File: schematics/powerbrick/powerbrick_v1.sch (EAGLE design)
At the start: 41 parts, among them U1 ATXMEGA128C3-AU, U2 TC1262-3.3VDB, U3 PRTR5V0U2X, U4 ULN2003LVPWR, U5 MCP9800A0T-M/OT

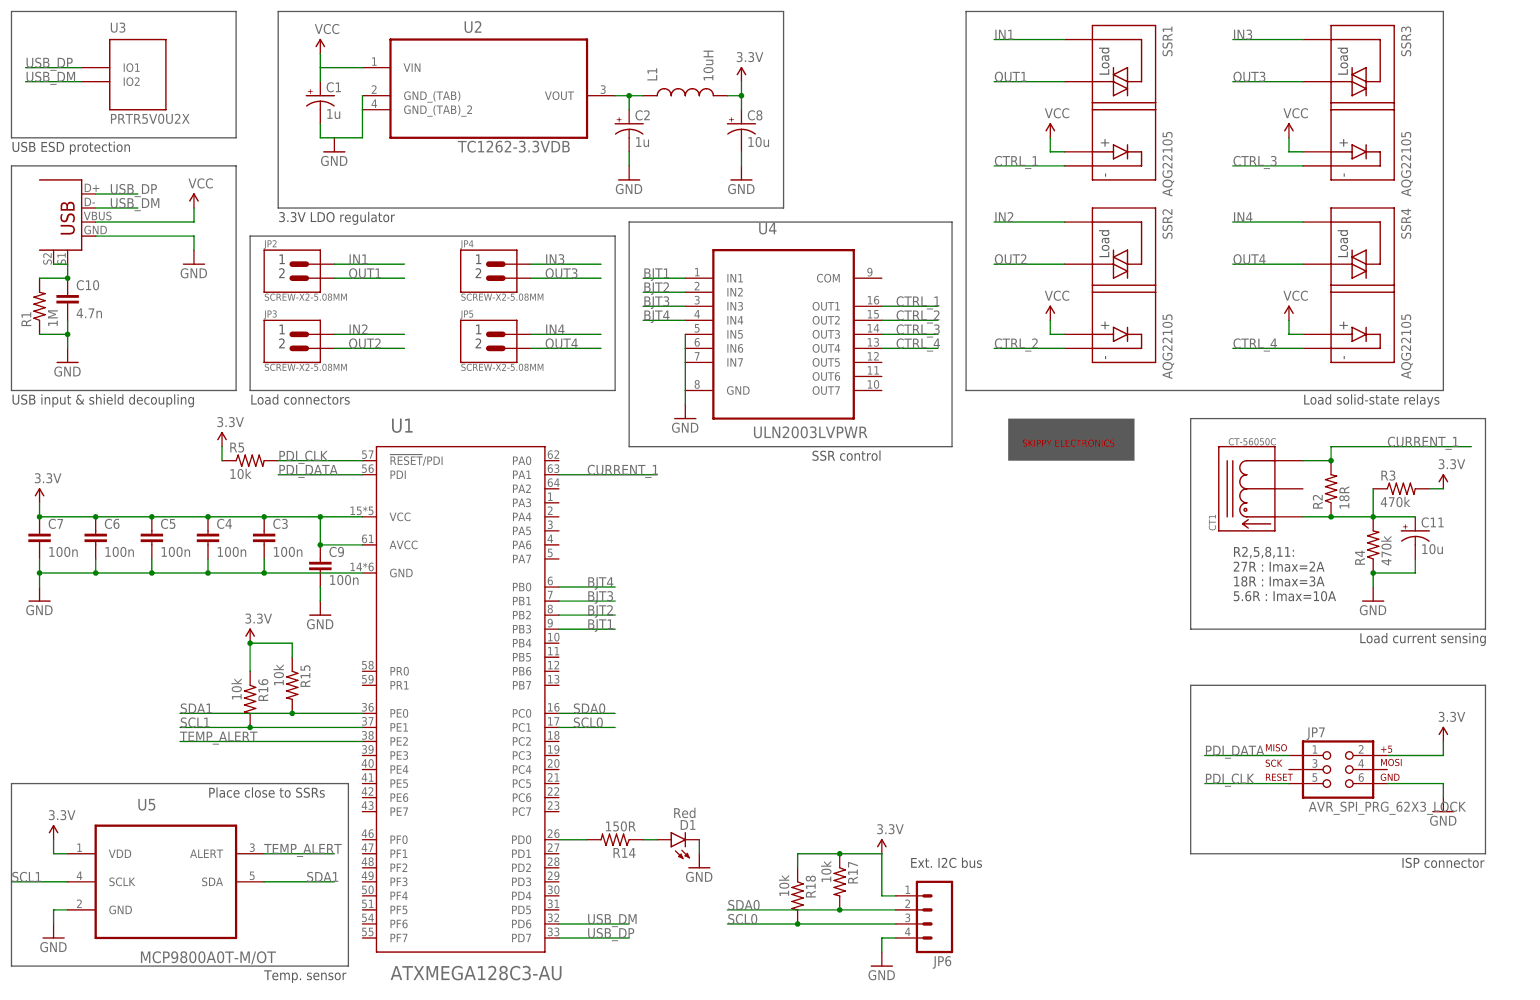
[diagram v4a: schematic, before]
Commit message: Replaced ISP connector - PCB draft
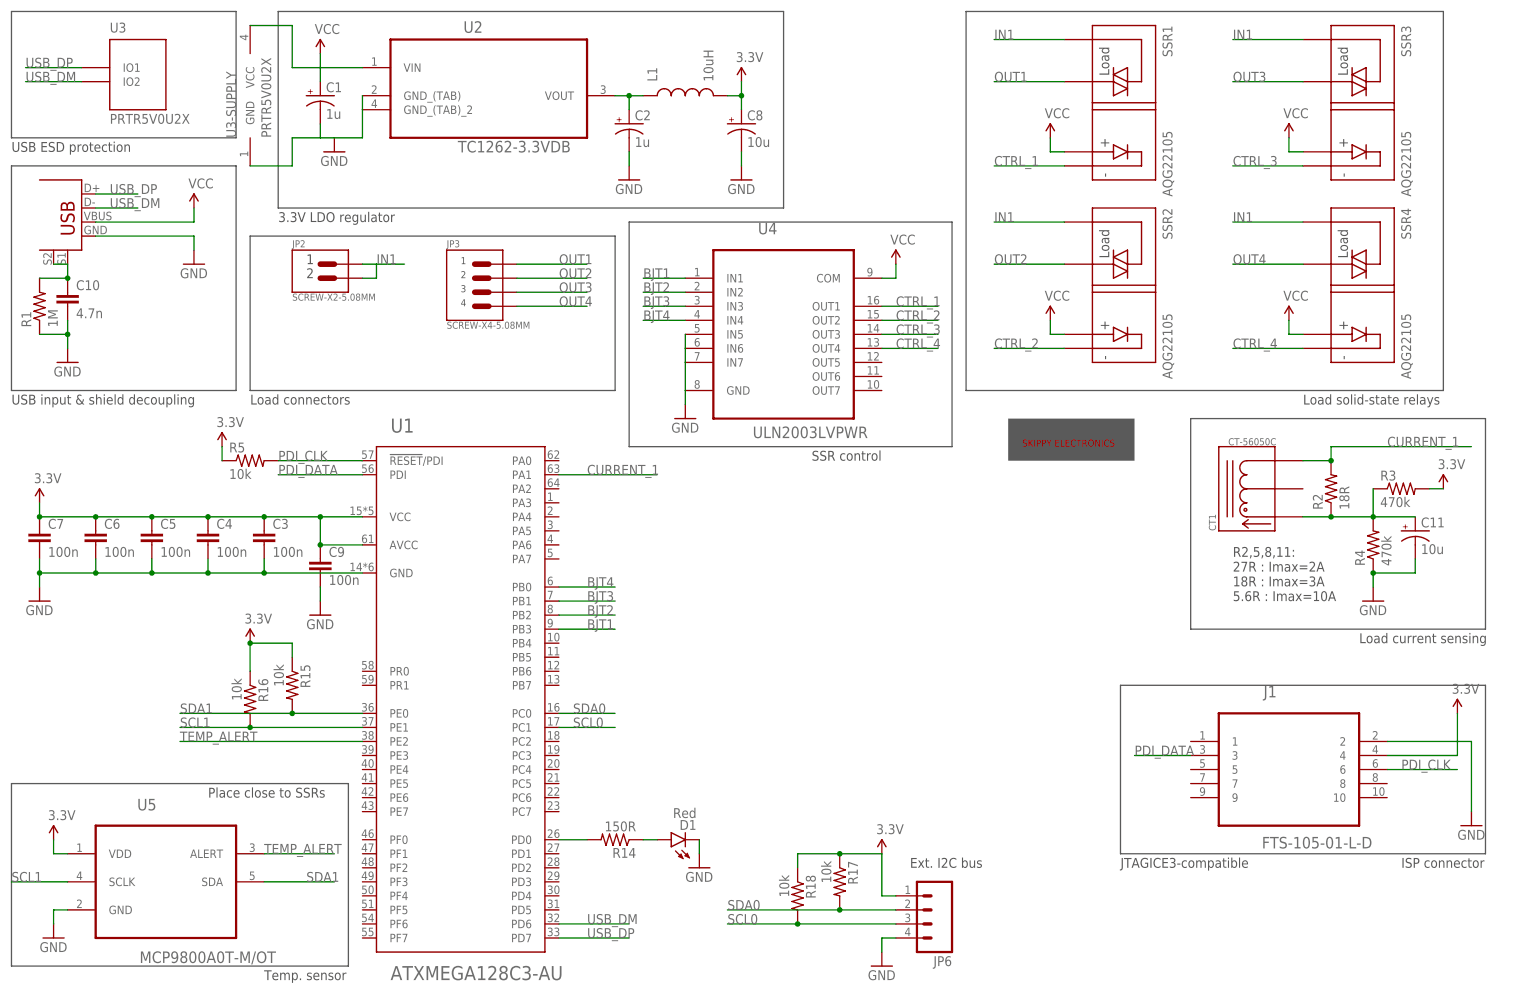
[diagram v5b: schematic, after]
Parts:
- removed JP4, JP5: SCREW-X2-5.08MM, Skippy-Connectors:SCREW-X2-5.08MM
- removed JP7: AVR_SPI_PRG_62X3_LOCK, SparkFun-Connectors:AVR_SPI_PRG_62X3_LOCK
- added J1: FTS-105-01-L-D, Skippy-Connectors:FTS-105-01-L-D
- JP3: value SCREW-X2-5.08MM -> SCREW-X4-5.08MM; device Skippy-Connectors:SCREW-X2-5.08MM -> Skippy-Connectors:SCREW-X4-5.08MM; OC_FARNELL 2315273 -> 2315275
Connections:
- removed net IN2: JP3.P$1, SSR2.P$1
- removed net IN3: JP4.P$1, SSR3.P$1
- removed net IN4: JP5.P$1, SSR4.P$1
- net 3.3V: now also J1.4; no longer JP7.2
- net GND: now also J1.2, U3-SUPPLY.GND; no longer JP7.6
- net IN1: now also JP2.P$2, SSR2.P$1, SSR3.P$1, SSR4.P$1
- net OUT1: now also JP3.P$1; no longer JP2.P$2
- net OUT3: now also JP3.P$3; no longer JP4.P$2
- net OUT4: now also JP3.P$4; no longer JP5.P$2
- net PDI_CLK: now also J1.6; no longer JP7.5
- net PDI_DATA: now also J1.3; no longer JP7.1
- net VCC: now also U3-SUPPLY.VCC, U4.COM
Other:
- note added: "JTAGICE3-compatible"
- moved on the sheet: JP2

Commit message: Added test points and HV separation milling
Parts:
- added C12, C13: 18p, SparkFun-Capacitors:CAP0805
- added R6, R7, R8, R9: Unfit, SparkFun-Passives:RESISTOR0805-RES
- added TP1, TP2, TP3: TEST-POINTTP_15TH_THRU, SparkFun-Passives:TEST-POINTTP_15TH_THRU
- added X1: 16MHz, Discrete:CRYSTAL'HC49S'
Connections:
- new net N$1: C12.2, U1.PR0, X1.2
- new net N$10: R9.2, SSR4.P$4
- new net N$13: R8.2, SSR2.P$4
- new net N$3: C13.2, U1.PR1, X1.1
- new net N$6: R6.2, SSR1.P$4
- new net N$9: R7.2, SSR3.P$4
- net 3.3V: now also TP2.1
- net CTRL_1: now also R6.1; no longer SSR1.P$4
- net CTRL_2: now also R8.1; no longer SSR2.P$4
- net CTRL_3: now also R7.1; no longer SSR3.P$4
- net CTRL_4: now also R9.1; no longer SSR4.P$4
- net GND: now also C12.1, C13.1, TP3.1
- net VCC: now also TP1.1
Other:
- moved on the sheet: R15, R16
